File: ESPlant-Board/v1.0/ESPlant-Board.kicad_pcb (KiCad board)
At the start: 2 copper layers, 29.2 x 158.5 mm, 24 parts, among them J2 Programmer, Q1 NPN, Q2 NPN, U1 ESP-12F

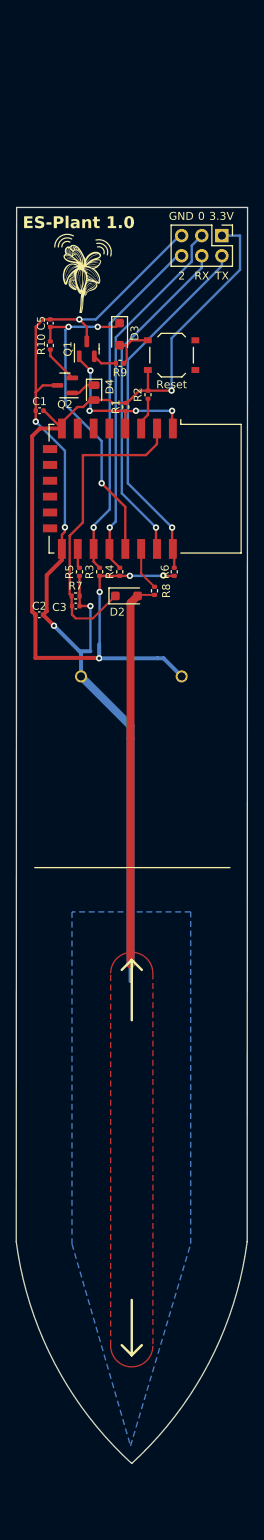
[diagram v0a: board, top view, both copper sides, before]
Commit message: Replace layout to use battery pack
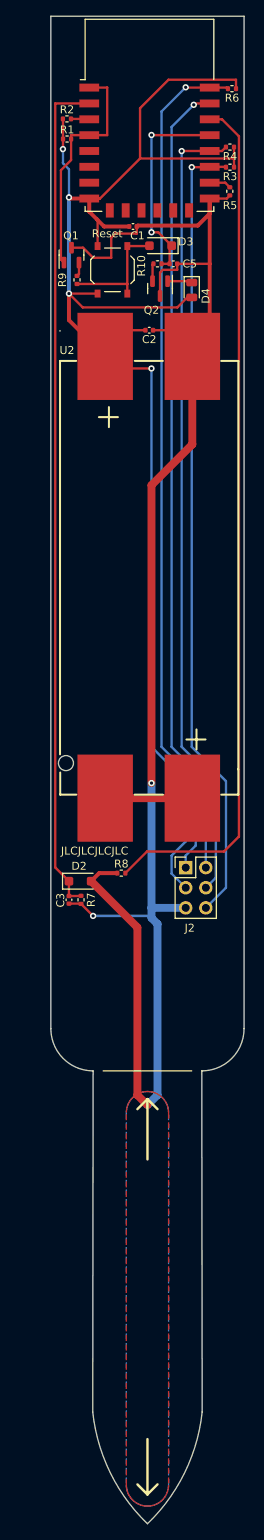
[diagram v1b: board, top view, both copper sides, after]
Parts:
- removed BT1: 2468, CustomFootprints:BAT_2468
- removed Reset1: Reset, CustomFootprints:SW_Push_1P1T_XKB_TS-1187A
- added SW1: Reset, CustomFootprints:SW_Push_1P1T_XKB_TS-1187A, F.Cu at (136.7, 40.2)
- added U2: BH-AAA-B5AK001, CustomFootprints:BAT-SMD_BH-AAA-B5AA001, F.Cu at (141.3, 79.0)
- G***: moved to B.Cu
- moved J2 79.9 mm to (145.9, 115.7), turned to 0 degrees
- moved R6 61.4 mm to (151.8, 17.4), turned to 180 degrees
- moved R4 55.4 mm to (151.5, 24.7), turned to 180 degrees
- moved R3 53.6 mm to (151.5, 27.3), turned to 180 degrees
- moved R5 51.6 mm to (151.5, 30.3)
- moved U1 47.1 mm to (141.3, 20.7), turned to 0 degrees
- moved C2 38.5 mm to (141.3, 47.8)
- moved R7 38.4 mm to (132.7, 119.7), turned to 90 degrees
- moved C3 37.1 mm to (131.2, 119.7), turned to 90 degrees
- moved D2 36.5 mm to (132.6, 117.4)
- moved R2 36.3 mm to (130.9, 21.2), turned to 0 degrees
- moved R8 35.9 mm to (137.8, 116.3), turned to 0 degrees
- moved R1 34.6 mm to (130.9, 23.7), turned to 0 degrees
- moved C1 26.1 mm to (139.3, 34.7), turned to 180 degrees
- moved D4 17.9 mm to (146.7, 42.8)
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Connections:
- J2 pad 1: +3.3V -> /TX
- J2 pad 2: /TX -> /RX
- J2 pad 3: /GPIO0 -> +3.3V
- J2 pad 4: /RX -> /GPIO0
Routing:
- net /GPIO5: track 5.48 -> 109.2 mm
- net +3.3V: track 119.2 -> 191.7 mm, vias 5 -> 4
- net /AD0: track 39.7 -> 106.6 mm
- net /TX: track 46.6 -> 107.5 mm
- net /RX: track 43.0 -> 101.3 mm
- net /GPIO2: track 44.6 -> 100.7 mm
- net /GPIO0: track 47.2 -> 101.1 mm
- net GND: track 131.3 -> 177.4 mm, vias 5 -> 2
- net /GPIO4: track 42.1 -> 26.3 mm, vias 3 -> 2
- net /SensorCapV: track 49.1 -> 34.9 mm
- net Net-(U2-+-Pad3): track 0.00 -> 11.0 mm
- net Net-(D3-A): track 6.45 -> 15.2 mm
- net /RST: track 22.4 -> 29.6 mm, vias 4 -> 0
- net Net-(Q2-B): track 4.73 -> 2.59 mm
- net Net-(U1-EN): track 4.11 -> 2.33 mm
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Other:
- board size 29.2 x 158.5 mm -> 24.4 x 190.2 mm
- board text added: "ES-Plant V1.0"
- board text removed: "0"
- board text removed: "2"
- board text removed: "3.3V"
- board text removed: "ES-Plant 1.0"
- board text removed: "GND"
- board text removed: "RX"
- board text removed: "TX"
